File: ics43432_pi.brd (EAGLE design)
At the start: 8.1 x 16.8 mm, 9 parts, among them U1 ICS43432

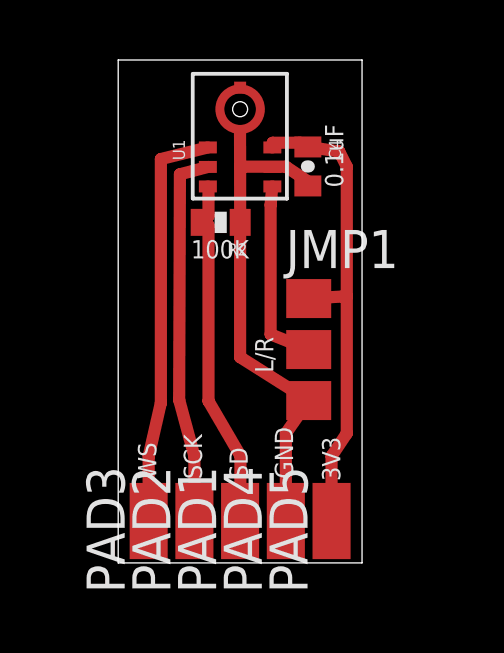
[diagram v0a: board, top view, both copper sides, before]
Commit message: added photos of assembled circuits
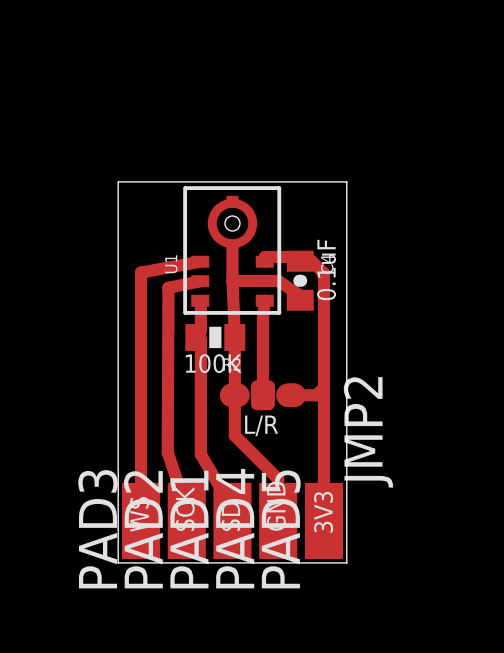
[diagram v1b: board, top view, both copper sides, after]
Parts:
- removed JMP1: 0R-JUMPA, jump-0r-smd:A0R-JMP
- added JMP2: 0R-JUMPC, jump-0r-smd:C0R-JMP
- moved R2 3.84 mm to (3.24, 7.52)
- moved C4 3.82 mm to (6.07, 9.41)
- moved U1 3.82 mm to (3.81, 10.4)
- moved PAD4 0.25 mm to (5.33, 1.40)
- moved PAD5 0.25 mm to (6.86, 1.40)
- moved PAD1 0.25 mm to (3.81, 1.40)
- moved PAD2 0.25 mm to (2.29, 1.40)
- moved PAD3 0.25 mm to (0.76, 1.40)
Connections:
- net GND: now also JMP2.3; no longer JMP1.3
- net LR: now also JMP2.2; no longer JMP1.2
- net VDD: now also JMP2.1; no longer JMP1.1
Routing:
- net GND: track 16.9 -> 12.2 mm
- net VDD: track 16.2 -> 11.8 mm
- net SD: track 11.7 -> 7.80 mm
- net SCK: track 12.6 -> 8.96 mm
- net WS: track 13.7 -> 10.3 mm
- net LR: track 6.30 -> 3.15 mm
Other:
- board size 8.1 x 16.8 mm -> 7.6 x 12.7 mm
